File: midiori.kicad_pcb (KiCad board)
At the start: 2 copper layers, 141 x 150 mm, 45 parts, among them J1 x68000_expansion, J2 Conn_ARM_JTAG_SWD_10, J4 Mini-DIN-5, U1 74LCX07, U10 ICE40HX1K-VQ100, U11 TLV73333PDBV, U2 AT25SF081-SSHD-X, U3 TLV73312PDBV, U4 SN74LVC8T245DWR, U5 SN74LVC8T245DWR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

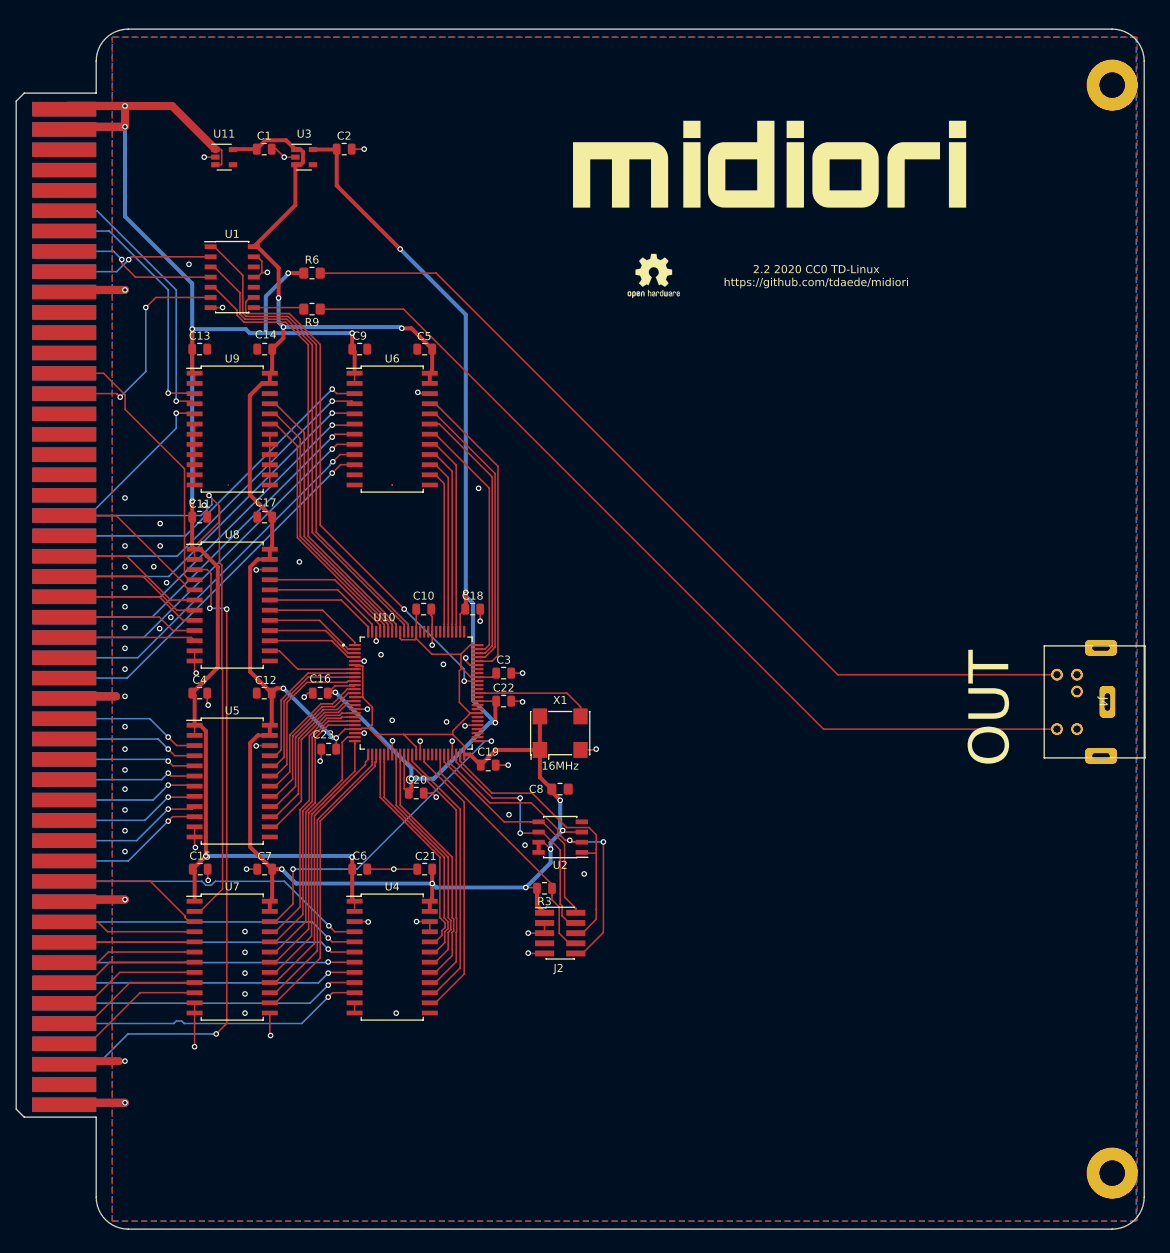
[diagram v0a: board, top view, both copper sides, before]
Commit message: Update and Refine
Tweak routing
1mm power traces
Shorter ground traces
Stitching vias
JLCPCB ready
Updated some footprints
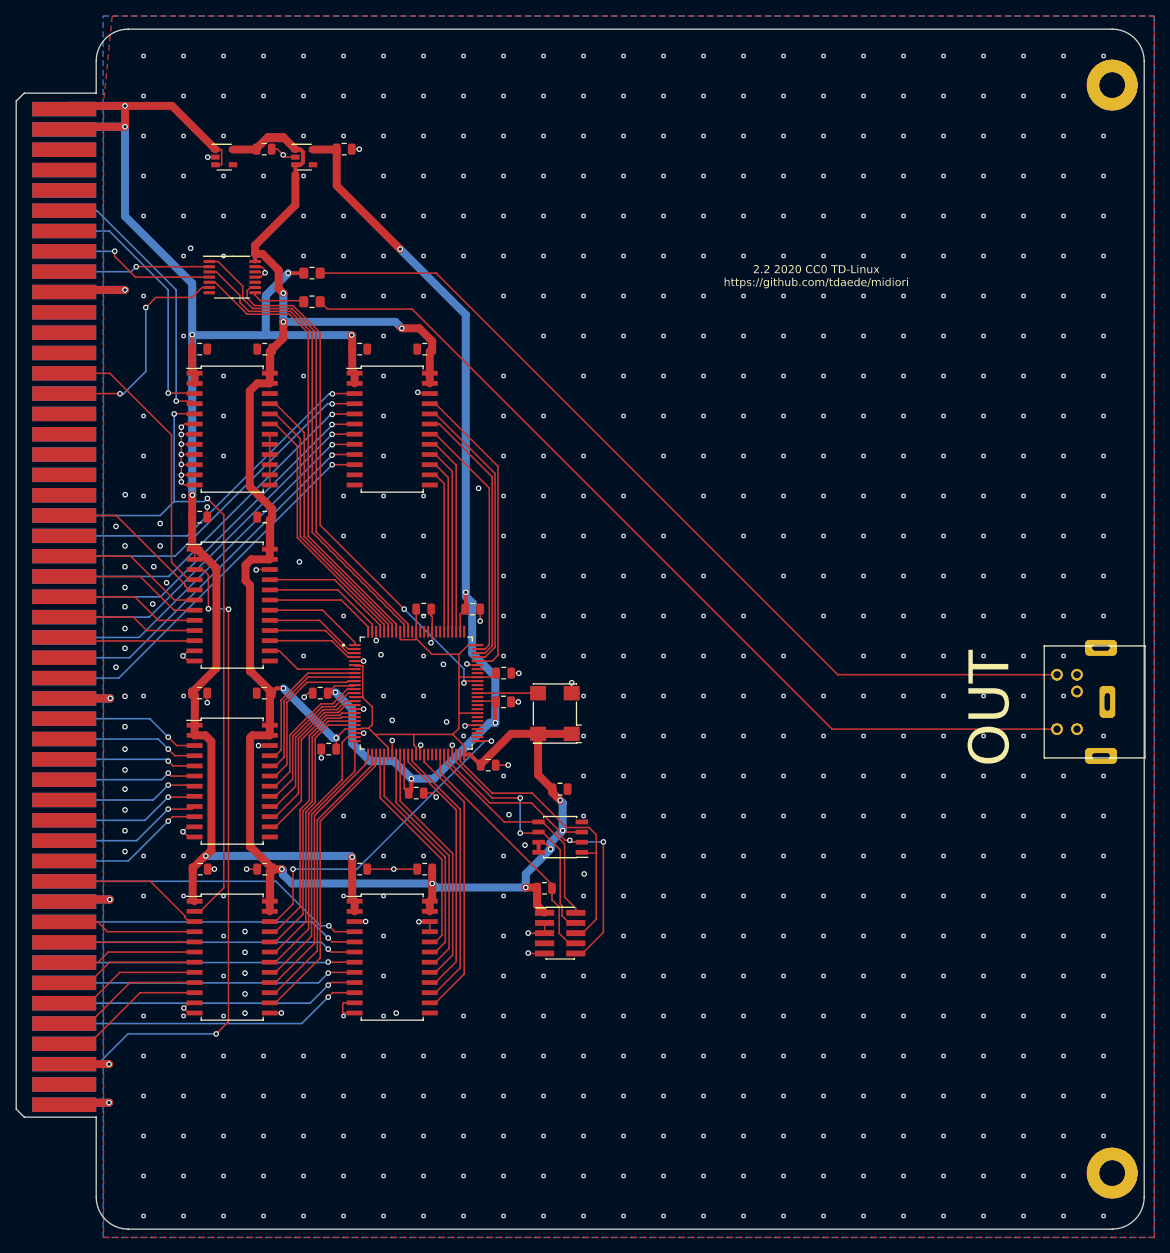
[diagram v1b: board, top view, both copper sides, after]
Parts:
- removed REF**: OSHW-Logo2_7.3x6mm_SilkScreen, Symbol:OSHW-Logo2_7.3x6mm_SilkScreen
- removed svg2mod: G***, x68k:midiori_logo
- C8: footprint Capacitor_SMD:C_0805_2012Metric_Pad1.15x1.40mm_HandSolder -> Capacitor_SMD:C_0805_2012Metric
- U1: footprint Package_SO:SOIC-14_3.9x8.7mm_P1.27mm -> Package_SO:TSSOP-14_4.4x5mm_P0.65mm
- moved X1 2.54 mm to (111.3, 124.5), turned to 90 degrees
- moved R9 0.92 mm to (81.0, 73.1)
- moved C22 0.10 mm to (104.9, 123.1)
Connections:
- J1 pad A13: Net-(J1-PadA13) -> unconnected-(J1-PadA13)
- J1 pad A14: Net-(J1-PadA14) -> unconnected-(J1-PadA14)
- J1 pad A15: Net-(J1-PadA15) -> unconnected-(J1-PadA15)
- J1 pad A16: Net-(J1-PadA16) -> unconnected-(J1-PadA16)
- J1 pad A17: Net-(J1-PadA17) -> unconnected-(J1-PadA17)
- J1 pad A18: Net-(J1-PadA18) -> unconnected-(J1-PadA18)
- J1 pad A19: Net-(J1-PadA19) -> unconnected-(J1-PadA19)
- J1 pad A2: Net-(J1-PadA2) -> unconnected-(J1-PadA2)
- J1 pad A20: Net-(J1-PadA20) -> unconnected-(J1-PadA20)
- J1 pad A22: Net-(J1-PadA22) -> unconnected-(J1-PadA22)
- J1 pad A23: Net-(J1-PadA23) -> unconnected-(J1-PadA23)
- J1 pad A29: Net-(J1-PadA29) -> unconnected-(J1-PadA29)
- J1 pad A31: Net-(J1-PadA31) -> unconnected-(J1-PadA31)
- J1 pad A32: Net-(J1-PadA32) -> unconnected-(J1-PadA32)
- J1 pad A33: Net-(J1-PadA33) -> unconnected-(J1-PadA33)
- J1 pad A34: Net-(J1-PadA34) -> unconnected-(J1-PadA34)
- J1 pad A35: Net-(J1-PadA35) -> unconnected-(J1-PadA35)
- J1 pad A38: Net-(J1-PadA38) -> unconnected-(J1-PadA38)
- J1 pad A39: Net-(J1-PadA39) -> unconnected-(J1-PadA39)
- J1 pad A40: Net-(J1-PadA40) -> unconnected-(J1-PadA40)
- J1 pad A42: Net-(J1-PadA42) -> unconnected-(J1-PadA42)
- J1 pad A43: Net-(J1-PadA43) -> unconnected-(J1-PadA43)
- J1 pad A44: Net-(J1-PadA44) -> unconnected-(J1-PadA44)
- J1 pad A45: Net-(J1-PadA45) -> unconnected-(J1-PadA45)
- J1 pad A46: Net-(J1-PadA46) -> unconnected-(J1-PadA46)
- J1 pad A47: Net-(J1-PadA47) -> unconnected-(J1-PadA47)
- J1 pad A48: Net-(J1-PadA48) -> unconnected-(J1-PadA48)
- J1 pad B2: Net-(J1-PadB2) -> unconnected-(J1-PadB2)
- J1 pad B31: Net-(J1-PadB31) -> unconnected-(J1-PadB31)
- J1 pad B32: Net-(J1-PadB32) -> unconnected-(J1-PadB32)
- J1 pad B33: Net-(J1-PadB33) -> unconnected-(J1-PadB33)
- J1 pad B34: Net-(J1-PadB34) -> unconnected-(J1-PadB34)
- J1 pad B35: Net-(J1-PadB35) -> unconnected-(J1-PadB35)
- J1 pad B36: Net-(J1-PadB36) -> unconnected-(J1-PadB36)
- J1 pad B37: Net-(J1-PadB37) -> unconnected-(J1-PadB37)
- J1 pad B38: Net-(J1-PadB38) -> unconnected-(J1-PadB38)
- J1 pad B39: Net-(J1-PadB39) -> unconnected-(J1-PadB39)
- J1 pad B4: Net-(J1-PadB4) -> unconnected-(J1-PadB4)
- J1 pad B40: Net-(J1-PadB40) -> unconnected-(J1-PadB40)
- J1 pad B46: Net-(J1-PadB46) -> unconnected-(J1-PadB46)
- J1 pad B47: Net-(J1-PadB47) -> unconnected-(J1-PadB47)
- J1 pad B48: Net-(J1-PadB48) -> unconnected-(J1-PadB48)
- J2 pad 7: Net-(J2-Pad7) -> unconnected-(J2-Pad7)
- J4 pad 1: Net-(J4-Pad1) -> unconnected-(J4-Pad1)
- J4 pad 3: Net-(J4-Pad3) -> unconnected-(J4-Pad3)
- U1 pad 10: Net-(U1-Pad10) -> unconnected-(U1-Pad10)
- U1 pad 12: Net-(U1-Pad12) -> unconnected-(U1-Pad12)
- U10 pad 41: Net-(U10-Pad41) -> unconnected-(U10-Pad41)
- U10 pad 42: Net-(U10-Pad42) -> unconnected-(U10-Pad42)
- U10 pad 43: Net-(U10-Pad43) -> unconnected-(U10-Pad43)
- U10 pad 52: Net-(U10-Pad52) -> unconnected-(U10-Pad52)
- U10 pad 53: Net-(U10-Pad53) -> unconnected-(U10-Pad53)
- U10 pad 54: Net-(U10-Pad54) -> unconnected-(U10-Pad54)
- U10 pad 56: Net-(U10-Pad56) -> unconnected-(U10-Pad56)
- U10 pad 57: Net-(U10-Pad57) -> unconnected-(U10-Pad57)
- U10 pad 59: Net-(U10-Pad59) -> unconnected-(U10-Pad59)
- U10 pad 60: Net-(U10-Pad60) -> unconnected-(U10-Pad60)
- U10 pad 62: Net-(U10-Pad62) -> unconnected-(U10-Pad62)
- U10 pad 64: Net-(U10-Pad64) -> unconnected-(U10-Pad64)
- U10 pad 65: Net-(U10-Pad65) -> unconnected-(U10-Pad65)
- U10 pad 68: Net-(U10-Pad68) -> unconnected-(U10-Pad68)
- U10 pad 69: Net-(U10-Pad69) -> unconnected-(U10-Pad69)
- U10 pad 76: Net-(U10-Pad76) -> unconnected-(U10-Pad76)
- U10 pad 82: Net-(U10-Pad82) -> unconnected-(U10-Pad82)
- U10 pad 83: Net-(U10-Pad83) -> unconnected-(U10-Pad83)
- U10 pad 85: Net-(U10-Pad85) -> unconnected-(U10-Pad85)
- U10 pad 86: Net-(U10-Pad86) -> unconnected-(U10-Pad86)
- U10 pad 87: Net-(U10-Pad87) -> unconnected-(U10-Pad87)
- U10 pad 89: Net-(U10-Pad89) -> unconnected-(U10-Pad89)
- U11 pad 4: Net-(U11-Pad4) -> unconnected-(U11-Pad4)
- U3 pad 4: Net-(U3-Pad4) -> unconnected-(U3-Pad4)
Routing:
- net +3V3: track 309.4 -> 363.8 mm
- net +5V: track 227.3 -> 263.7 mm
- net /IDDIR: track 103.6 -> 85.9 mm
- net GND: track 166.7 -> 150.8 mm, vias 81 -> 693
- net Net-(U10-Pad63): track 14.8 -> 7.56 mm
- net /DB3: track 17.4 -> 14.3 mm
- net /DB2: track 17.9 -> 14.8 mm
- net /DB1: track 18.4 -> 15.3 mm
- net /DB0: track 18.9 -> 15.8 mm
- net /AB18: track 49.4 -> 46.3 mm
- net /sck: track 32.4 -> 30.1 mm
- net /ss: track 38.4 -> 36.4 mm
- net /irq2: track 61.7 -> 60.1 mm
- net +1V2: track 133.1 -> 134.5 mm
- net /d2: track 34.0 -> 32.7 mm
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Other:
- net class Default removed
